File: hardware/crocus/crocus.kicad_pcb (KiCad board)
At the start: 4 copper layers, 70.7 x 53.3 mm, 49 parts, among them J1 NEIGHBOR1, J2 NEIGHBOR2, J7 BONUS_ROW, P1 RP-SMA, P2 EXPANSION, T1 BALUN, U1 nRF24L01+, U2 PCA9674, Y1 XTAL

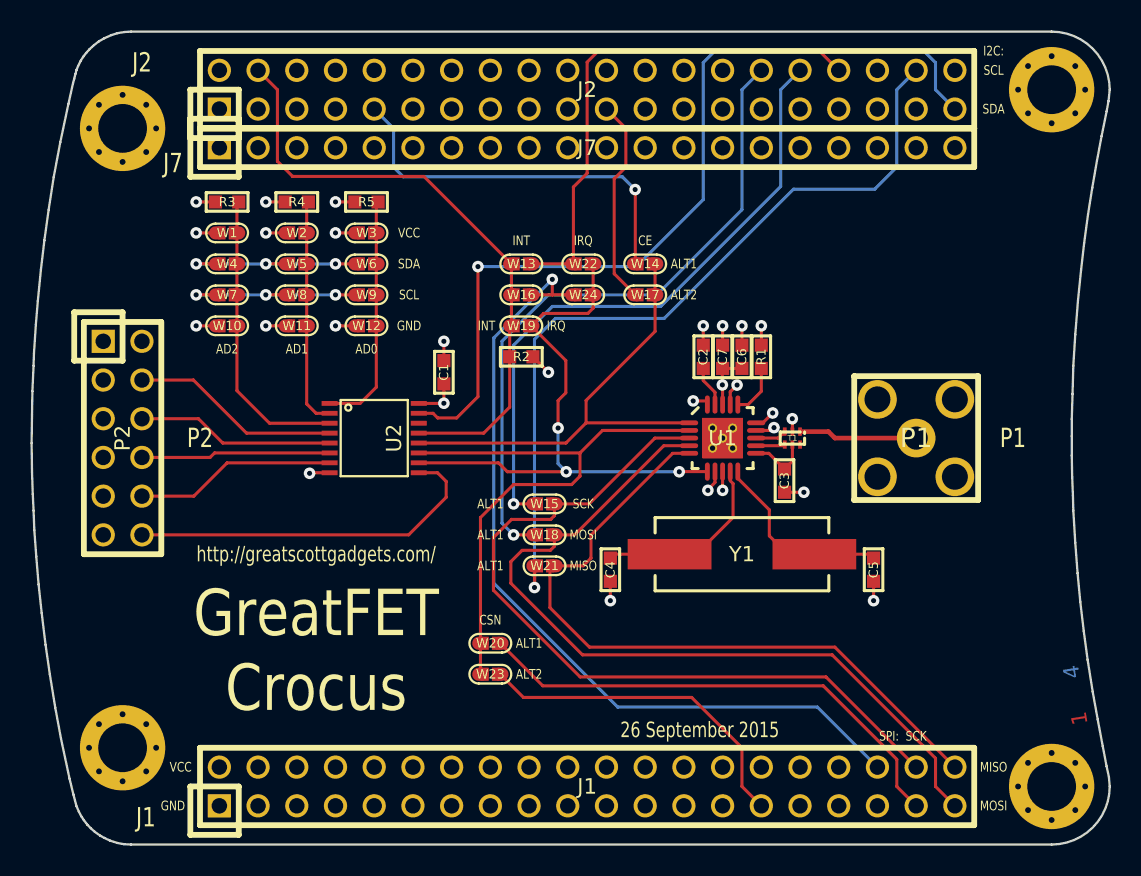
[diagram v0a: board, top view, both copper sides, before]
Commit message: crocus: switched from vertical to PCB edge RP-SMA connector
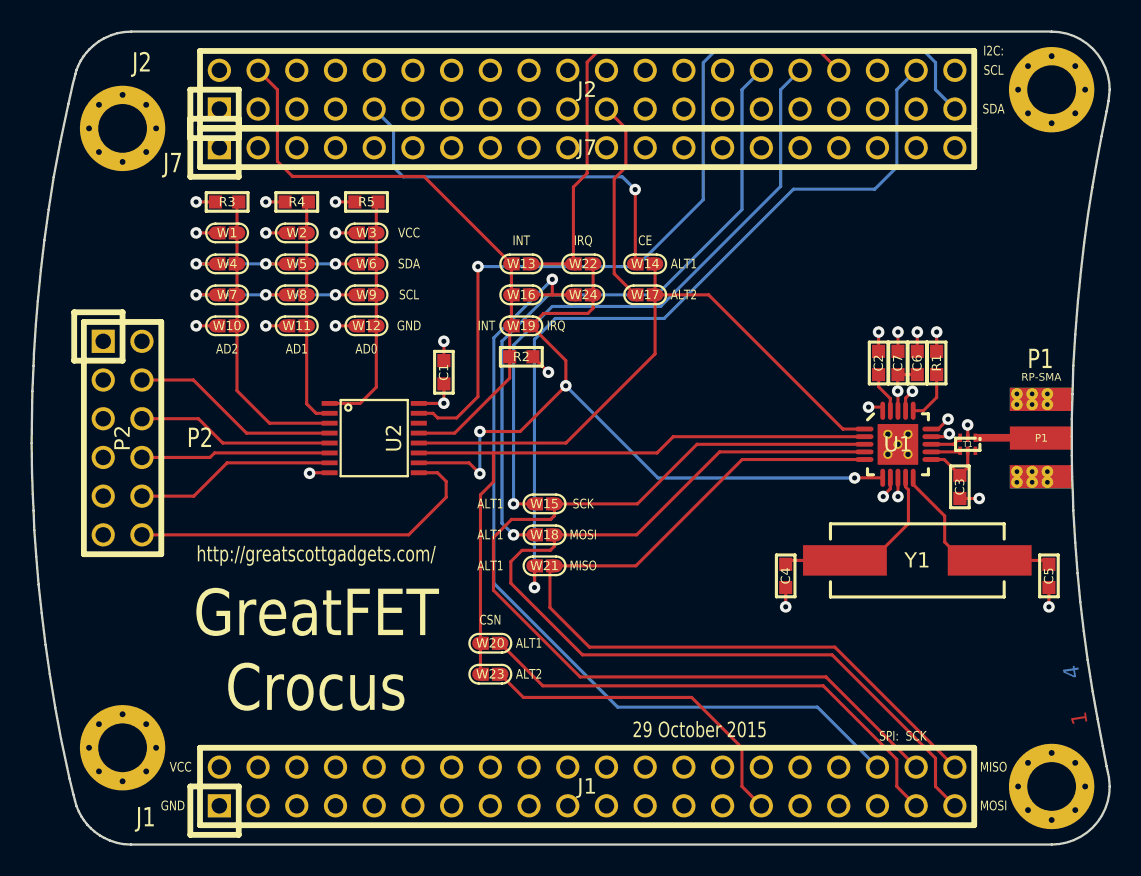
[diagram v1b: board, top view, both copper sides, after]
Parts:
- P1: footprint gsg-modules:SMA-VERTICAL -> gsg-modules:SMA-EDGE
- moved C2 11.5 mm to (165.2, 90.3)
- moved C3 11.5 mm to (170.5, 98.5)
- moved C5 11.5 mm to (176.4, 104.3)
- moved C7 11.5 mm to (166.4, 90.3)
- moved R1 11.5 mm to (169.0, 90.3)
- moved U1 11.5 mm to (166.4, 95.7)
- moved C4 11.5 mm to (159.1, 104.3)
- moved C6 11.5 mm to (167.7, 90.3)
- moved T1 11.5 mm to (171.0, 95.7)
- moved Y1 11.5 mm to (167.7, 103.3)
- moved P1 10.2 mm to (177.9, 95.2), turned to 180 degrees
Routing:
- net /IRQ: track 37.6 -> 49.6 mm, vias 3 -> 4
- net /SCK: track 52.0 -> 63.3 mm
- net /MOSI: track 53.0 -> 64.3 mm
- net /MISO: track 46.4 -> 57.2 mm
- net /CE: track 30.6 -> 41.2 mm
- net /CSN: track 37.8 -> 44.6 mm
- net /RF: track 7.80 -> 4.30 mm
- net /INT: track 40.8 -> 39.6 mm
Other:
- board text added: "29 October 2015"
- board text removed: "26 September 2015"

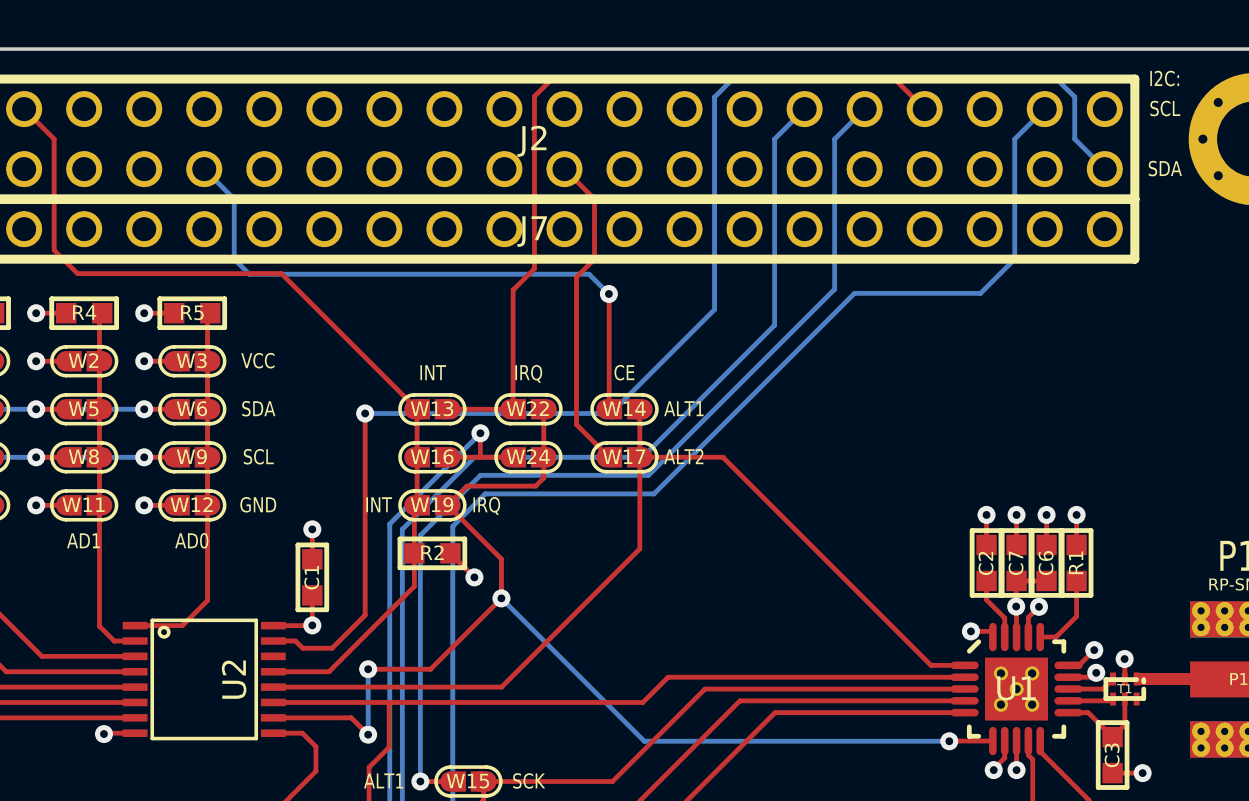
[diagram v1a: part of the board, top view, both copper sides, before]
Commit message: Crocus: Corrected I2C connection errors, thanks to docprofsky!
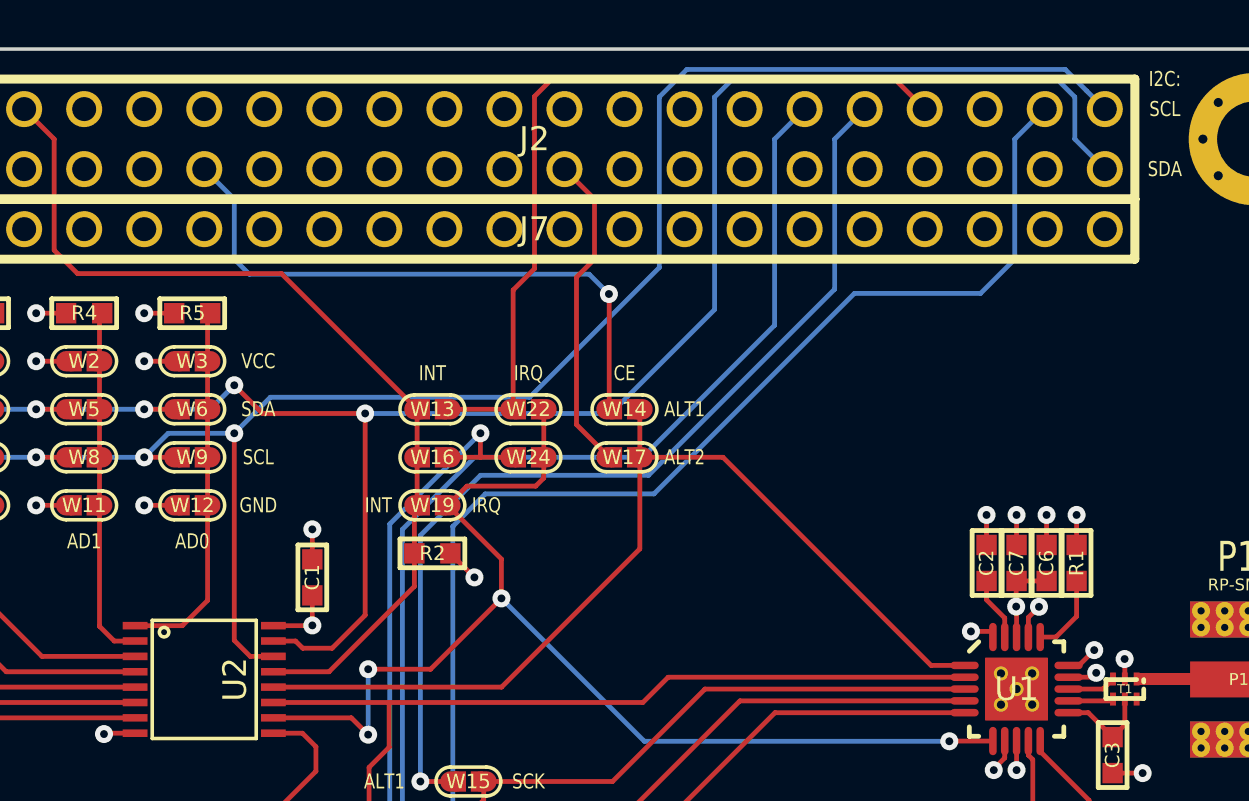
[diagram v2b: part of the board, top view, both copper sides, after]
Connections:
- U2 pad 14: /I2C0_SDL -> /I2C0_SCL
- W4 pad 1: /SDA -> /I2C0_SDA
- W5 pad 1: /SDA -> /I2C0_SDA
- W6 pad 1: /SDA -> /I2C0_SDA
- W7 pad 1: /SCL -> /I2C0_SCL
- W8 pad 1: /SCL -> /I2C0_SCL
- W9 pad 1: /SCL -> /I2C0_SCL
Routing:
- net /I2C0_SCL: track 0.00 -> 76.6 mm, vias 0 -> 4
- net /I2C0_SDA: track 58.2 -> 81.7 mm, vias 1 -> 5
- net /SCL: track 13.6 -> 0.00 mm, vias 3 -> 0
- net /SDA: track 13.3 -> 0.00 mm, vias 3 -> 0

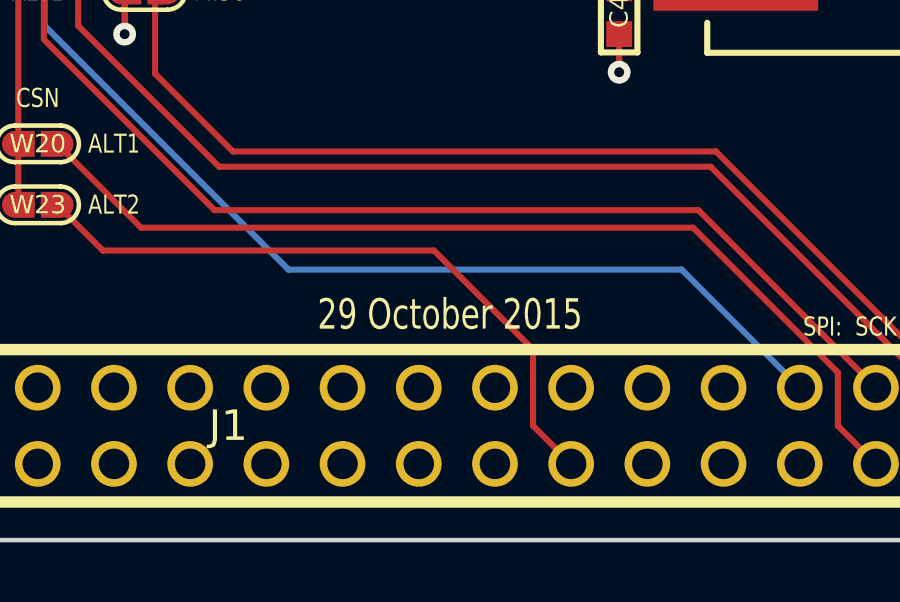
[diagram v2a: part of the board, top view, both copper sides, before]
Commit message: Crocus: updated date on silkscreen
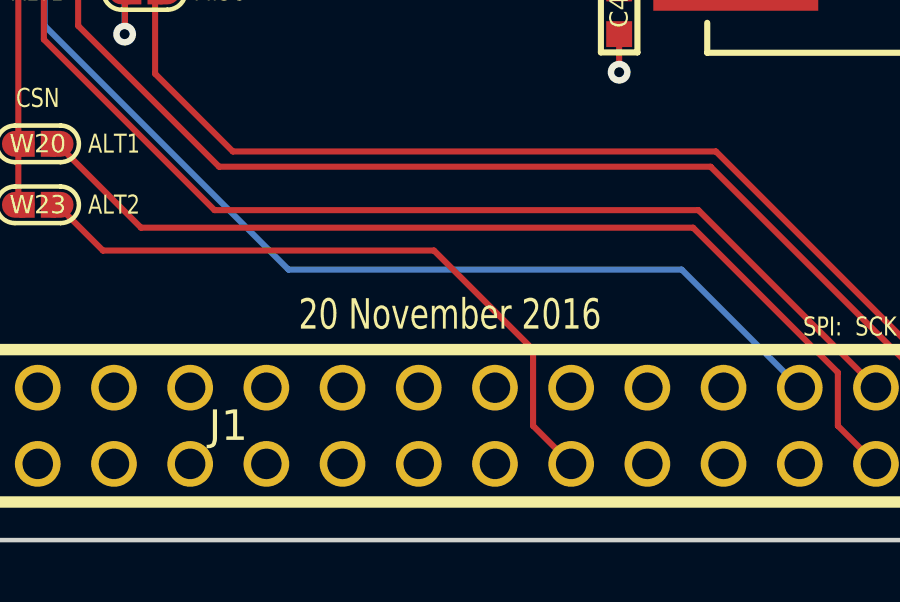
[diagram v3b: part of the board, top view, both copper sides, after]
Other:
- board text added: "20 November 2016"
- board text removed: "29 October 2015"
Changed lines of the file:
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@@
     (links 209)
     (no_connects 2)
-    (area 109.525999 68.504999 180.415001 121.995001)
+    (area 107.95 66.04 279.525801 124.460001)
     (thickness 1.6)
     (drawings 144)
@@
   (gr_line (start 177.9016 92.3544) (end 177.8508 94.0054) (angle 90) (layer Edge.Cuts) (width 0.15))
   (gr_line (start 177.9524 90.5002) (end 177.9016 92.3544) (angle 90) (layer Edge.Cuts) (width 0.15))
-  (gr_text "29 October 2015" (at 153.4414 114.4016) (layer F.SilkS)
+  (gr_text "20 November 2016" (at 153.4414 114.4016) (layer F.SilkS)
     (effects (font (size 1.016 0.762) (thickness 0.1524)))
   )
